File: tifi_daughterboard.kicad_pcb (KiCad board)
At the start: 2 copper layers, 57.4 x 32.3 mm, 28 parts, among them J1 SSW-110-23-F-D, J2 SSW-110-23-F-D, J3 SM04B-SRSS-TB(LF)(SN), J4 SSW-103-02-T-S-RA, J5 PH2-04-UA, Q1 BSS138LT1G, U1 SGP40-D-R4, U2 SHT40-AD1B-R3

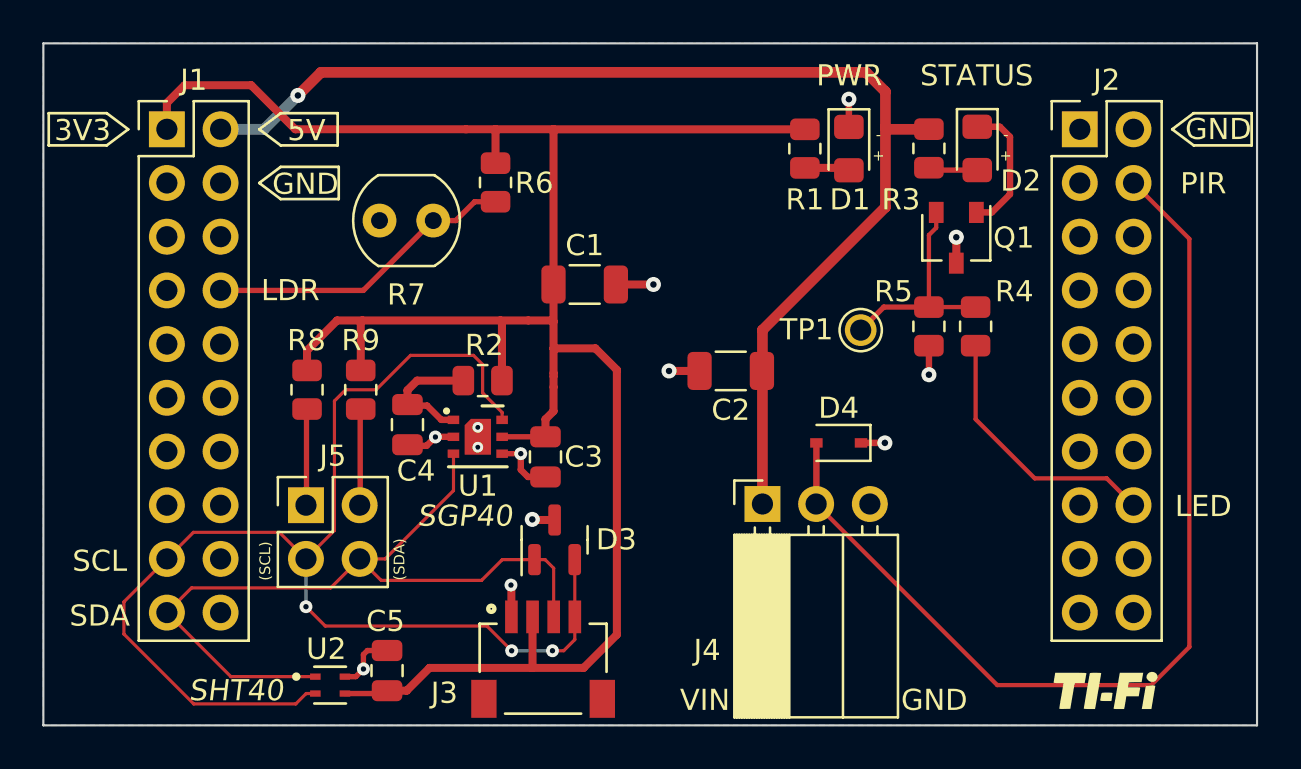
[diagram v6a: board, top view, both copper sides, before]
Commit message: Add board fiducials and pad to SGP40 symbol.
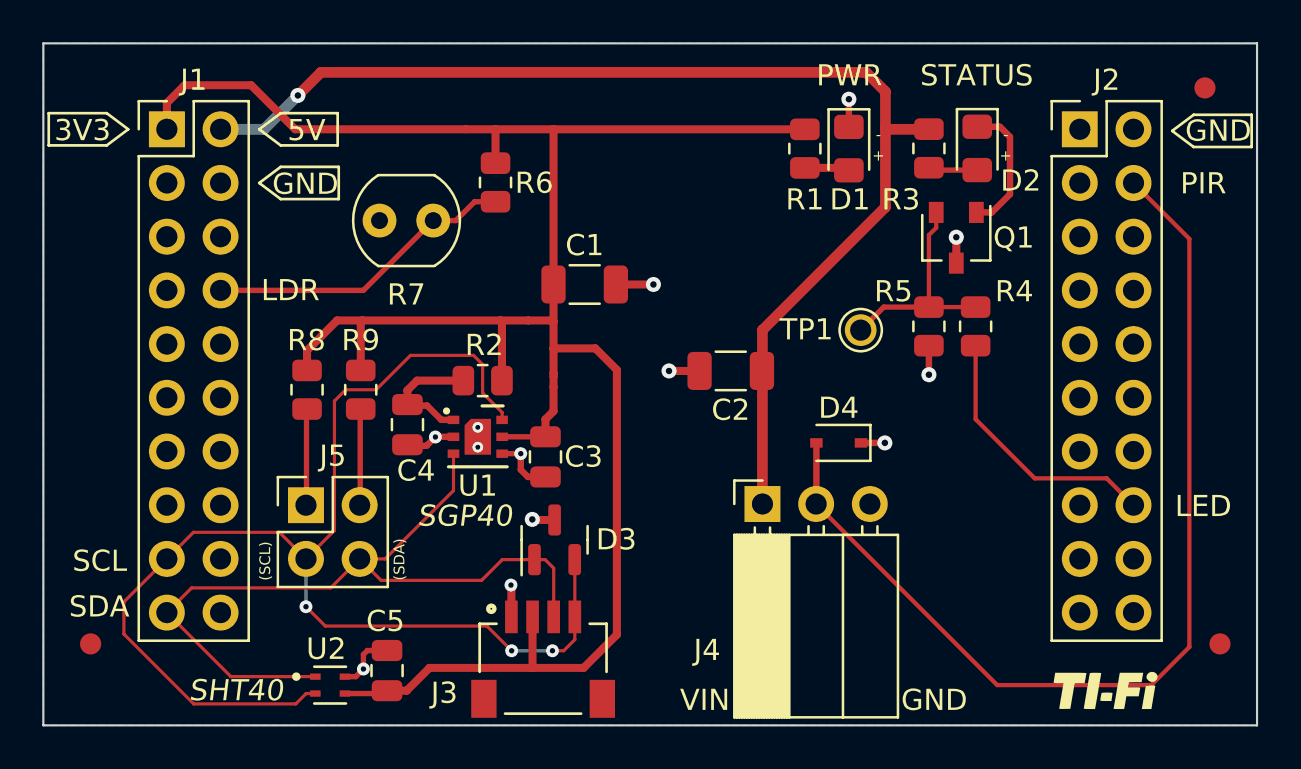
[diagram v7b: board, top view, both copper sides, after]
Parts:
- added FID1: Fiducial, Fiducial:Fiducial_1mm_Mask2mm, F.Cu at (118.3, 98.0)
- added FID2: Fiducial, Fiducial:Fiducial_1mm_Mask2mm, F.Cu at (171.7, 98.0)
- added FID3: Fiducial, Fiducial:Fiducial_1mm_Mask2mm, F.Cu at (171.0, 71.7)
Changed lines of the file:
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@@
     )
+  )
+  (footprint "Fiducial:Fiducial_1mm_Mask2mm" (layer "F.Cu")
+    (at 118.3132 98)
+    (descr "Circular Fiducial, 1mm bare copper, 2mm soldermask opening (Level A)")
+    (tags "fiducial")
+    (property "Sheetfile" "tifi_daughterboard.kicad_sch")
+    (property "Sheetname" "")
+    (property "exclude_from_bom" "")
+    (attr smd exclude_from_bom)
+    (fp_text reference "FID1" (at 0 -2) (layer "F.SilkS") hide
+      (effects (font (size 1 1) (thickness 0.15)))
+    )
+    (fp_text value "Fiducial" (at 0 2) (layer "F.Fab")
+      (effects (font (size 1 1) (thickness 0.15)))
+    )
+    (fp_text user "${REFERENCE}" (at 0 0) (layer "F.Fab")
+      (effects (font (size 0.4 0.4) (thickness 0.06)))
+    )
+    (fp_circle (center 0 0) (end 1.25 0) (layer "F.CrtYd") (width 0.05) (fill none))
+    (fp_circle (center 0 0) (end 1 0) (layer "F.Fab") (width 0.1) (fill none))
+    (pad "" smd circle (at 0 0) (size 1 1) (layers "F.Cu" "F.Mask")
+      (solder_mask_margin 0.5) (clearance 0.5))
   )
   (footprint "Capacitor_SMD:C_1206_3216Metric" (layer "F.Cu")
@@
       (rotate (xyz 0 0 0))
     )
+  )
+  (footprint "Fiducial:Fiducial_1mm_Mask2mm" (layer "F.Cu")
+    (at 171.7294 98)
+    (descr "Circular Fiducial, 1mm bare copper, 2mm soldermask opening (Level A)")
+    (tags "fiducial")
+    (property "Sheetfile" "tifi_daughterboard.kicad_sch")
+    (property "Sheetname" "")
+    (property "exclude_from_bom" "")
+    (attr smd exclude_from_bom)
+    (fp_text reference "FID2" (at 0 -2) (layer "F.SilkS") hide
+      (effects (font (size 1 1) (thickness 0.15)))
+    )
+    (fp_text value "Fiducial" (at 0 2) (layer "F.Fab")
+      (effects (font (size 1 1) (thickness 0.15)))
+    )
+    (fp_text user "${REFERENCE}" (at 0 0) (layer "F.Fab")
+      (effects (font (size 0.4 0.4) (thickness 0.06)))
+    )
+    (fp_circle (center 0 0) (end 1.25 0) (layer "F.CrtYd") (width 0.05) (fill none))
+    (fp_circle (center 0 0) (end 1 0) (layer "F.Fab") (width 0.1) (fill none))
+    (pad "" smd circle (at 0 0) (size 1 1) (layers "F.Cu" "F.Mask")
+      (solder_mask_margin 0.5) (clearance 0.5))
   )
   (footprint "Resistor_SMD:R_0805_2012Metric" (layer "F.Cu")
@@
     (pad "7" smd roundrect (at 0 0) (size 1.25 1.7) (layers "F.Cu" "F.Mask") (roundrect_rratio 0)
       (chamfer_ratio 0.24) (chamfer top_left)
-      (net 2 "GND"))
+      (net 2 "GND") (pinfunction "MP") (pintype "unspecified"))
     (model "${KICAD6_3DMODEL_DIR}/Package_DFN_QFN.3dshapes/DFN-6-1EP_2x2mm_P0.5mm_EP0.61x1.42mm.wrl" hide
       (offset (xyz 0 0 0))
@@
       (rotate (xyz 0 0 0))
     )
+  )
+  (footprint "Fiducial:Fiducial_1mm_Mask2mm" (layer "F.Cu")
+    (at 171.0182 71.7042)
+    (descr "Circular Fiducial, 1mm bare copper, 2mm soldermask opening (Level A)")
+    (tags "fiducial")
+    (property "Sheetfile" "tifi_daughterboard.kicad_sch")
+    (property "Sheetname" "")
+    (property "exclude_from_bom" "")
+    (attr smd exclude_from_bom)
+    (fp_text reference "FID3" (at 0 -2) (layer "F.SilkS") hide
+      (effects (font (size 1 1) (thickness 0.15)))
+    )
+    (fp_text value "Fiducial" (at 0 2) (layer "F.Fab")
+      (effects (font (size 1 1) (thickness 0.15)))
+    )
+    (fp_text user "${REFERENCE}" (at 0 0) (layer "F.Fab")
+      (effects (font (size 0.4 0.4) (thickness 0.06)))
+    )
+    (fp_circle (center 0 0) (end 1.25 0) (layer "F.CrtYd") (width 0.05) (fill none))
+    (fp_circle (center 0 0) (end 1 0) (layer "F.Fab") (width 0.1) (fill none))
+    (pad "" smd circle (at 0 0) (size 1 1) (layers "F.Cu" "F.Mask")
+      (solder_mask_margin 0.5) (clearance 0.5))
   )
   (footprint "TiFi Footprints:D_SOD-323" (layer "F.Cu")
@@
     (fp_circle (center 0 0) (end 1 0) (layer "F.SilkS") (width 0.12) (fill none))
     (fp_circle (center 0 0) (end 1.3 0) (layer "F.CrtYd") (width 0.05) (fill none))
-    (pad "1" thru_hole circle (at 0 0) (size 1.5 1.5) (drill 1) (layers *.Cu *.Mask)
+    (pad "1" thru_hole circle (at 0 0) (size 1.5 1.5) (drill 1) (property pad_prop_testpoint) (layers *.Cu *.Mask)
       (net 42 "Net-(Q1-Pad2)") (pinfunction "1") (pintype "passive"))
   )
@@
   (gr_poly
     (pts
-      (xy 169.4688 73.66)
-      (xy 170.4848 74.422)
-      (xy 173.228 74.422)
-      (xy 173.228 72.898)
-      (xy 170.4848 72.898)
-    ) (layer "B.SilkS") (width 0.127) (fill none))
-  (gr_poly
-    (pts
       (xy 120.0912 73.66)
       (xy 119.0752 74.422)
@@
   (gr_poly
     (pts
-      (xy 169.4688 73.66)
-      (xy 170.4848 72.898)
-      (xy 173.228 72.898)
-      (xy 173.228 74.422)
-      (xy 170.4848 74.422)
+      (xy 169.4688 73.7362)
+      (xy 170.4848 72.9742)
+      (xy 173.228 72.9742)
+      (xy 173.228 74.4982)
+      (xy 170.4848 74.4982)
     ) (layer "F.SilkS") (width 0.127) (fill none))
   (gr_poly
@@
     (effects (font (size 1 1) (thickness 0.15)))
   )
-  (gr_text "GND" (at 171.6532 73.66) (layer "F.SilkS")
+  (gr_text "GND" (at 171.6532 73.7362) (layer "F.SilkS")
     (effects (font (size 1 1) (thickness 0.15)))
   )
@@
     (effects (font (size 1 1) (thickness 0.15)))
   )
-  (gr_text "SDA" (at 118.745 96.6724) (layer "F.SilkS")
+  (gr_text "SDA" (at 118.7196 96.2406) (layer "F.SilkS")
     (effects (font (size 1 1) (thickness 0.15)))
   )

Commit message: Schematic cleanup, minor board fixes.
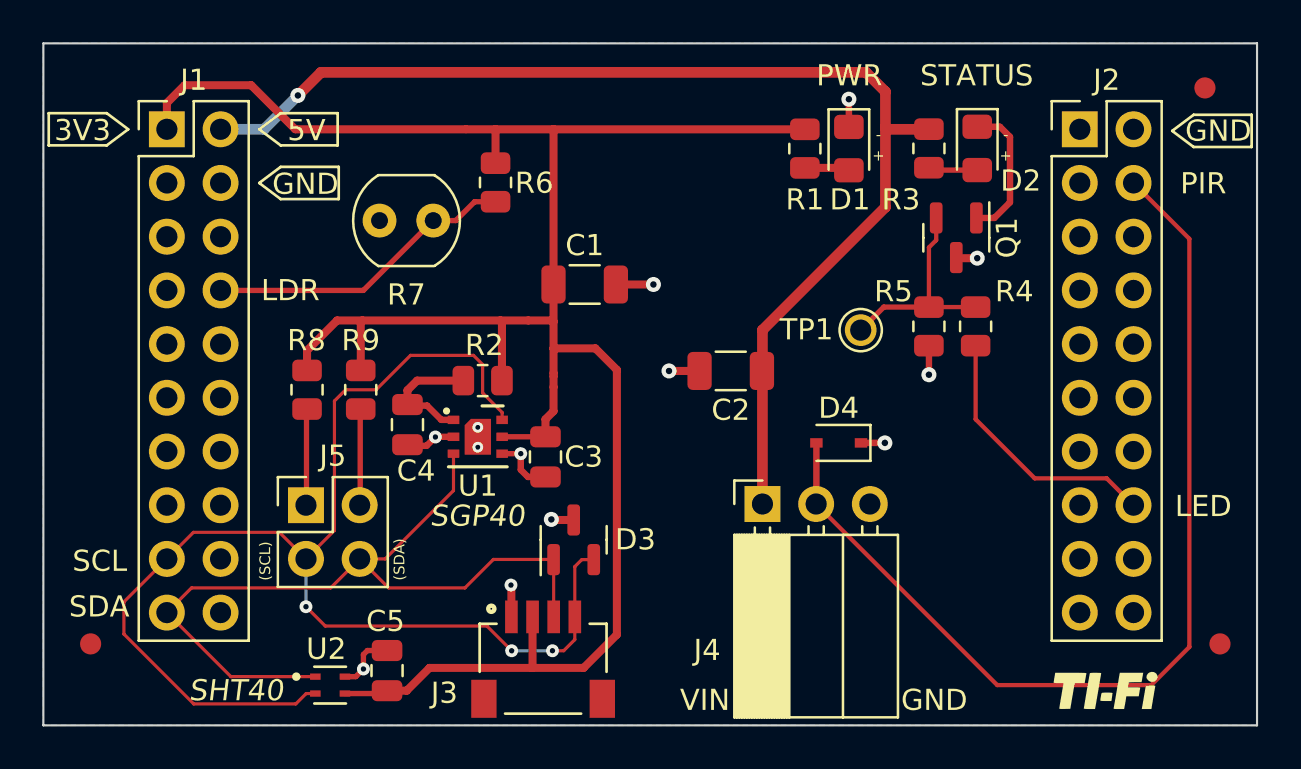
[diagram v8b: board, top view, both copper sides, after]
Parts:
- Q1: footprint Package_TO_SOT_SMD:SOT-23W -> Package_TO_SOT_SMD:SOT-23
- moved D3 0.90 mm to (141.2, 93.1)
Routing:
- net I2C_SCL: track 61.6 -> 62.3 mm
- net I2C_SDA: track 38.4 -> 39.0 mm
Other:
- rule pad_to_mask_clearance: 0.0635 -> 0
